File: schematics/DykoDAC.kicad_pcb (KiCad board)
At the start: 2 copper layers, 99.2 x 99.8 mm, 147 parts, among them J1 AC Input, J2 AudioJack, J3 USB_B, J4 OLED, J5 Debug, J6 Conn_01x05, J7 Conn_01x04, J8 Conn_01x05, J9 Conn_01x04, SW1 EC11B152420G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

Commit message: update
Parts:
- added C70: 10u, Capacitor_Tantalum_SMD:CP_EIA-3216-18_Kemet-A, F.Cu at (95.4, 135.4)
- C14, C15, C26, C29, C33, C35, C42, C50, C52, C59, C64, C65, C9: footprint Capacitors_Tantalum_SMD:CP_Tantalum_Case-A_EIA-3216-18_Reflow -> Capacitor_Tantalum_SMD:CP_EIA-3216-18_Kemet-A
- C32, C49, C7, C8: footprint Capacitors_Tantalum_SMD:CP_Tantalum_Case-D_EIA-7343-31_Reflow -> Capacitor_Tantalum_SMD:CP_EIA-7343-31_Kemet-D
- J2: footprint Connect:Stereo_Jack_3.5mm_Switch_Ledino_KB3SPRS -> kamtar:StereoJack_3.5mm_Lumberg
- moved L3 0.66 mm to (93.5, 134.7)
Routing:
- net +3V3: track 137.7 -> 157.8 mm
- net Net-(J2-Pad3): track 33.5 -> 21.9 mm
- net Net-(J2-Pad2): track 12.4 -> 21.5 mm
- net GND: track 105.2 -> 107.9 mm, vias 694 -> 878
- net /DykoDAC_CS4398/3V3_CS: track 30.5 -> 29.9 mm
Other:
- board text added: "Kamtar 2020"
- board text removed: "Kamtar 2019"

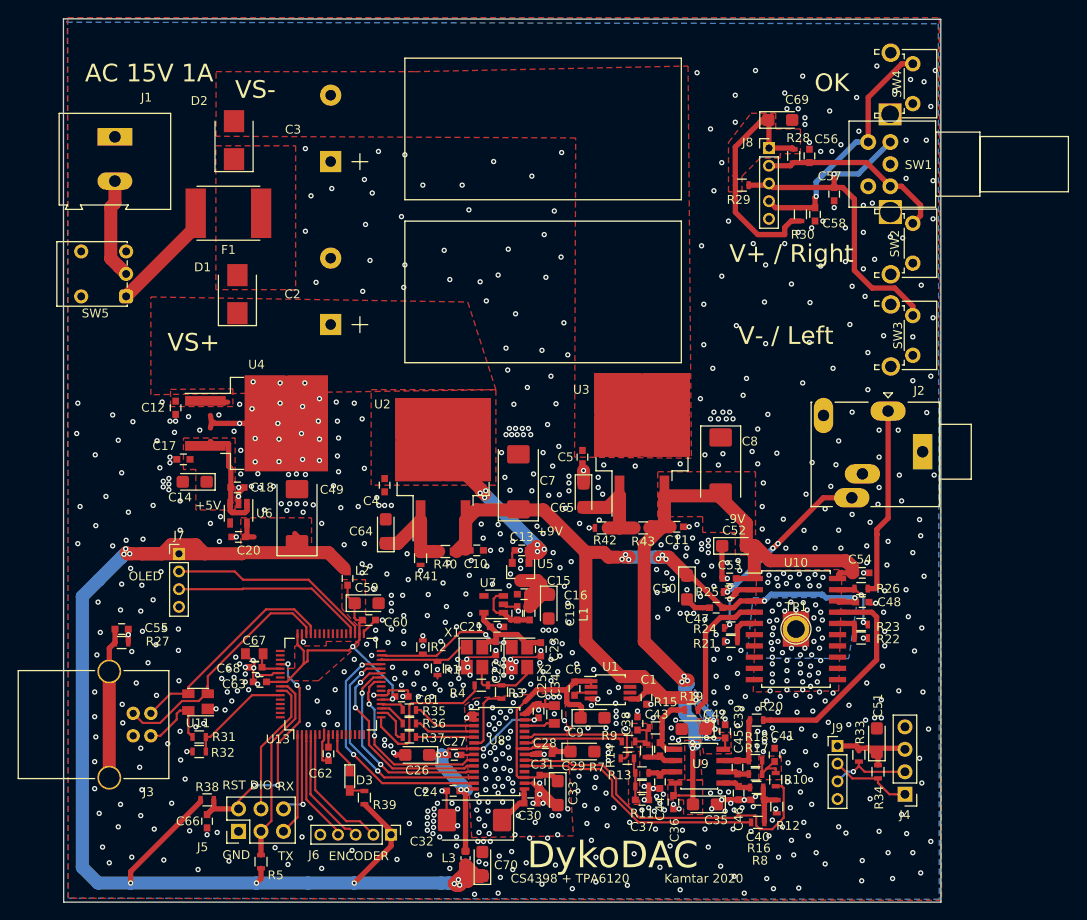
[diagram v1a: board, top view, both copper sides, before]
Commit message: lm317 fix
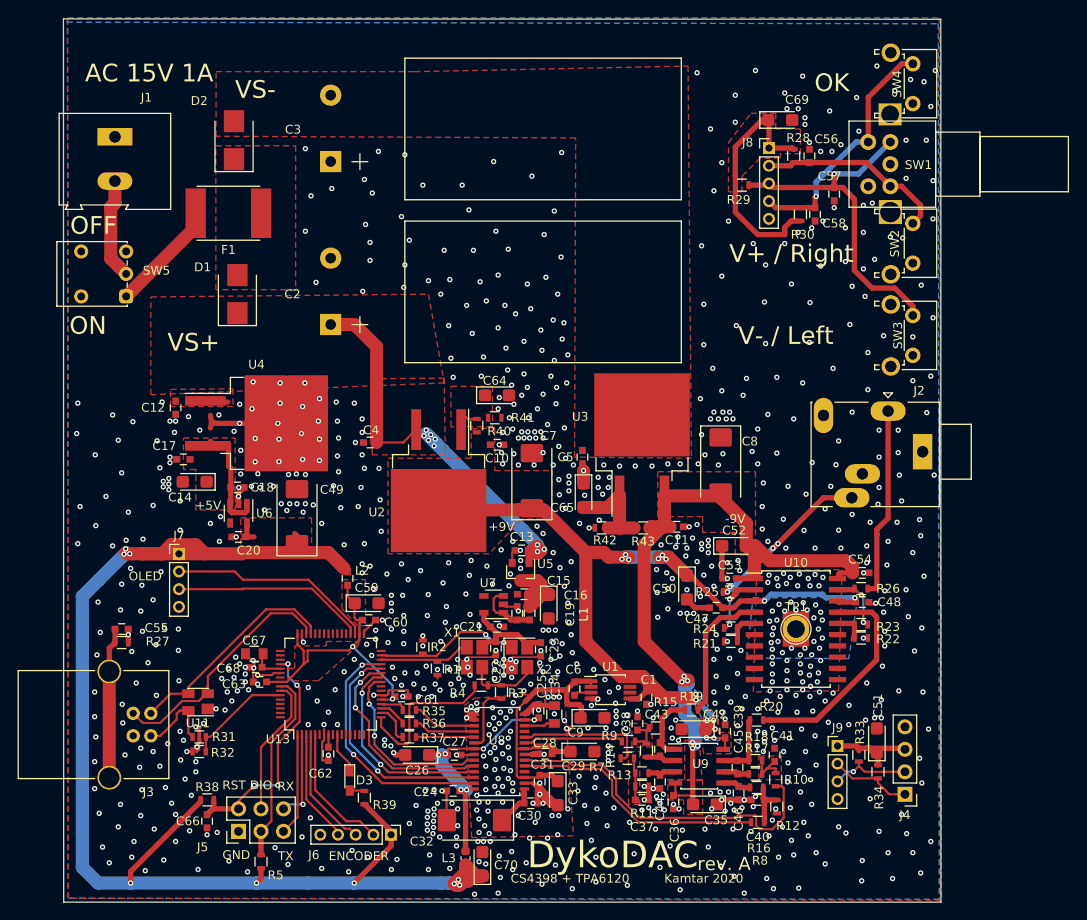
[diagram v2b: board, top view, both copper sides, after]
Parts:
- SW5: value SW_SPDT -> PWR_SWITCH
- U2, U3: footprint TO_SOT_Packages_SMD:TO-263-2 -> Package_TO_SOT_SMD:TO-263-2
- moved C64 19.9 mm to (97.0, 82.4), turned to 0 degrees
- moved R41 18.0 mm to (96.8, 85.0), turned to 0 degrees
- moved R40 14.7 mm to (94.7, 85.9), turned to 90 degrees
- moved C10 12.2 mm to (97.0, 88.0)
- moved C4 5.10 mm to (82.7, 87.8), turned to 180 degrees
- moved C7 1.53 mm to (101.0, 92.1)
- moved U2 1.37 mm to (90.4, 92.1), turned to 270 degrees
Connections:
- U2 pad 2: VS_POS -> +9V
- U2 pad 3: +9V -> VS_POS
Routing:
- net VS_POS: track 19.4 -> 46.4 mm, vias 6 -> 9
- net GND: track 107.9 -> 118.2 mm, vias 878 -> 954
- net +9V: track 110.9 -> 102.0 mm
- net Net-(C64-Pad1): track 10.6 -> 4.07 mm
- added copper zone on F.Cu, net Net-(C64-Pad1)
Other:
- board text added: "OFF"
- board text added: "ON"
- board text added: "rev. A"

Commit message: updated fuse
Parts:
- F1: footprint Fuse_Holders_and_Fuses:Fuse_SMD2920 -> kamtar:UNIFuse_SMD2920
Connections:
- J2 pad 4: Net-(J2-Pad4) -> (no net)
- J2 pad 5: Net-(J2-Pad5) -> (no net)
- SW5 pad 3: Net-(SW5-Pad3) -> (no net)
- U1 pad 6: Net-(U1-Pad6) -> (no net)
- U1 pad 7: Net-(U1-Pad7) -> (no net)
- U13 pad 11: Net-(U13-Pad11) -> (no net)
- U13 pad 12: Net-(U13-Pad12) -> (no net)
- U13 pad 13: Net-(U13-Pad13) -> (no net)
- U13 pad 14: Net-(U13-Pad14) -> (no net)
- U13 pad 15: Net-(U13-Pad15) -> (no net)
- U13 pad 16: Net-(U13-Pad16) -> (no net)
- U13 pad 23: Net-(U13-Pad23) -> (no net)
- U13 pad 24: Net-(U13-Pad24) -> (no net)
- U13 pad 32: Net-(U13-Pad32) -> (no net)
- U13 pad 37: Net-(U13-Pad37) -> (no net)
- U13 pad 38: Net-(U13-Pad38) -> (no net)
- U13 pad 39: Net-(U13-Pad39) -> (no net)
- U13 pad 40: Net-(U13-Pad40) -> (no net)
- U13 pad 41: Net-(U13-Pad41) -> (no net)
- U13 pad 42: Net-(U13-Pad42) -> (no net)
- U13 pad 43: Net-(U13-Pad43) -> (no net)
- U13 pad 44: Net-(U13-Pad44) -> (no net)
- U13 pad 49: Net-(U13-Pad49) -> (no net)
- U13 pad 50: Net-(U13-Pad50) -> (no net)
- U13 pad 51: Net-(U13-Pad51) -> (no net)
- U13 pad 55: Net-(U13-Pad55) -> (no net)
- U13 pad 6: Net-(U13-Pad6) -> (no net)
- U13 pad 60: Net-(U13-Pad60) -> (no net)
- U13 pad 61: Net-(U13-Pad61) -> (no net)
- U13 pad 62: Net-(U13-Pad62) -> (no net)
- U13 pad 63: Net-(U13-Pad63) -> (no net)
- U13 pad 64: Net-(U13-Pad64) -> (no net)
- U13 pad 9: Net-(U13-Pad9) -> (no net)
- U6 pad 4: Net-(U6-Pad4) -> (no net)
- U7 pad 4: Net-(U7-Pad4) -> (no net)
- U8 pad 18: Net-(U8-Pad18) -> (no net)
- U8 pad 25: Net-(U8-Pad25) -> (no net)
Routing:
- net GND: vias 954 -> 957

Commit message: added vias
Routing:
- net GND: vias 957 -> 960
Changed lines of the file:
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@@
     (thickness 1.6)
     (drawings 26)
-    (tracks 2032)
+    (tracks 2035)
     (zones 0)
     (modules 148)
@@
       (padsonsilk false)
       (subtractmaskfromsilk false)
-      (outputformat 1)
+      (outputformat 4)
       (mirror false)
       (drillshape 0)
@@
     (add_net "Net-(J2-Pad2)")
     (add_net "Net-(J2-Pad3)")
-    (add_net "Net-(J2-Pad4)")
-    (add_net "Net-(J2-Pad5)")
     (add_net "Net-(J3-Pad1)")
     (add_net "Net-(J4-Pad1)")
@@
     (add_net "Net-(R36-Pad1)")
     (add_net "Net-(R37-Pad1)")
-    (add_net "Net-(SW5-Pad3)")
-    (add_net "Net-(U1-Pad6)")
-    (add_net "Net-(U1-Pad7)")
-    (add_net "Net-(U13-Pad11)")
-    (add_net "Net-(U13-Pad12)")
-    (add_net "Net-(U13-Pad13)")
-    (add_net "Net-(U13-Pad14)")
-    (add_net "Net-(U13-Pad15)")
-    (add_net "Net-(U13-Pad16)")
-    (add_net "Net-(U13-Pad23)")
-    (add_net "Net-(U13-Pad24)")
-    (add_net "Net-(U13-Pad32)")
-    (add_net "Net-(U13-Pad37)")
-    (add_net "Net-(U13-Pad38)")
-    (add_net "Net-(U13-Pad39)")
-    (add_net "Net-(U13-Pad40)")
-    (add_net "Net-(U13-Pad41)")
-    (add_net "Net-(U13-Pad42)")
-    (add_net "Net-(U13-Pad43)")
-    (add_net "Net-(U13-Pad44)")
-    (add_net "Net-(U13-Pad49)")
-    (add_net "Net-(U13-Pad50)")
-    (add_net "Net-(U13-Pad51)")
-    (add_net "Net-(U13-Pad55)")
-    (add_net "Net-(U13-Pad6)")
-    (add_net "Net-(U13-Pad60)")
-    (add_net "Net-(U13-Pad61)")
-    (add_net "Net-(U13-Pad62)")
-    (add_net "Net-(U13-Pad63)")
-    (add_net "Net-(U13-Pad64)")
-    (add_net "Net-(U13-Pad9)")
-    (add_net "Net-(U6-Pad4)")
-    (add_net "Net-(U7-Pad4)")
-    (add_net "Net-(U8-Pad18)")
-    (add_net "Net-(U8-Pad25)")
     (add_net OSC_EN_1)
     (add_net OSC_EN_2)
@@
   (via (at 128.397 121.412) (size 0.6) (drill 0.3) (layers F.Cu B.Cu) (net 1))
   (via (at 128.524 129.159) (size 0.6) (drill 0.3) (layers F.Cu B.Cu) (net 1))
-  (via (at 109.601 122.047) (size 0.6) (drill 0.3) (layers F.Cu B.Cu) (net 1))
-  (via (at 109.601 122.809) (size 0.6) (drill 0.3) (layers F.Cu B.Cu) (net 1))
-  (via (at 109.601 123.698) (size 0.6) (drill 0.3) (layers F.Cu B.Cu) (net 1))
+  (via (at 109.4232 122.0216) (size 0.6) (drill 0.3) (layers F.Cu B.Cu) (net 1))
+  (via (at 109.347 122.809) (size 0.6) (drill 0.3) (layers F.Cu B.Cu) (net 1))
+  (via (at 109.3724 123.5456) (size 0.6) (drill 0.3) (layers F.Cu B.Cu) (net 1))
   (via (at 110.49 119.507) (size 0.6) (drill 0.3) (layers F.Cu B.Cu) (net 1))
   (via (at 110.49 118.745) (size 0.6) (drill 0.3) (layers F.Cu B.Cu) (net 1))
@@
   (via (at 139.7508 121.412) (size 0.6) (drill 0.3) (layers F.Cu B.Cu) (net 1))
   (via (at 141.5796 121.3612) (size 0.6) (drill 0.3) (layers F.Cu B.Cu) (net 1))
+  (via (at 106.934 121.9708) (size 0.6) (drill 0.3) (layers F.Cu B.Cu) (net 1))
+  (via (at 106.934 122.682) (size 0.6) (drill 0.3) (layers F.Cu B.Cu) (net 1))
+  (via (at 106.934 123.3932) (size 0.6) (drill 0.3) (layers F.Cu B.Cu) (net 1))
   (segment (start 122.797 122.219) (end 122.588 122.428) (width 0.25) (layer F.Cu) (net 2))
   (segment (start 122.184 121.146) (end 122.809 121.146) (width 0.25) (layer F.Cu) (net 2))

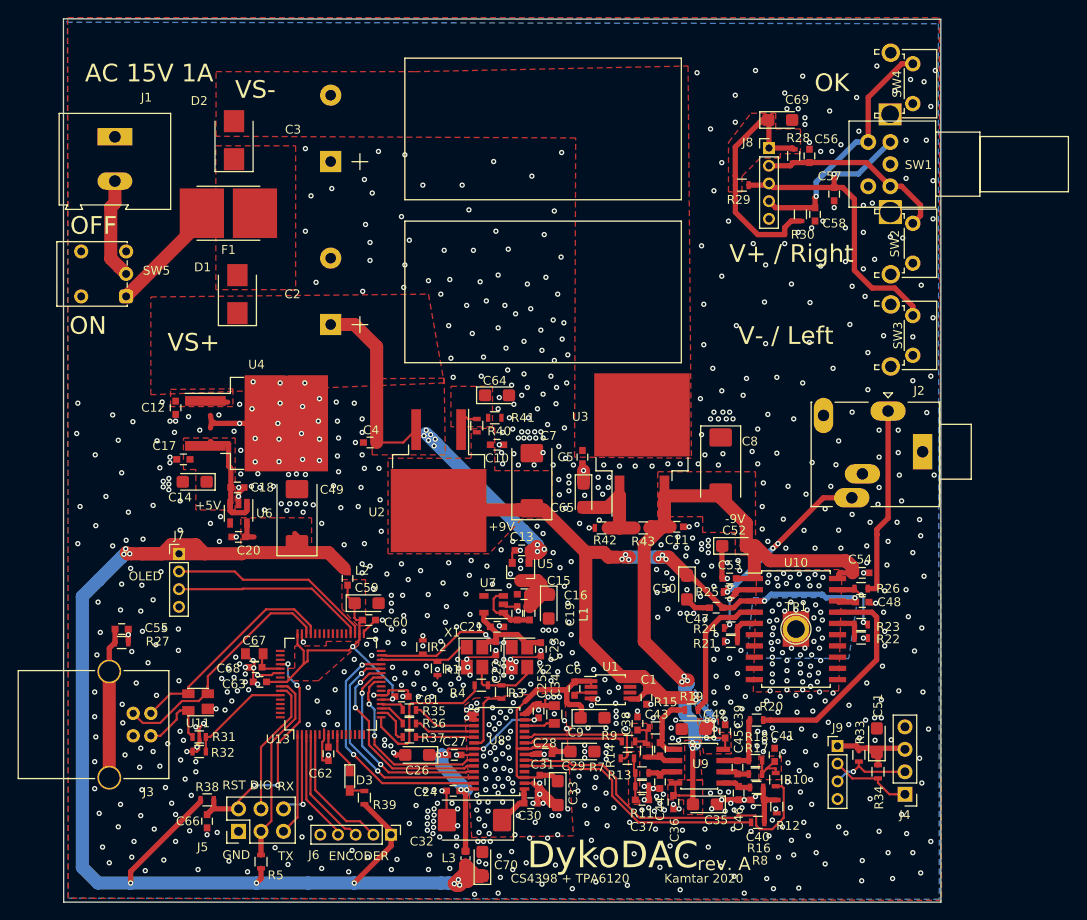
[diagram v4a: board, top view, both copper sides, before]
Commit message: ldo change
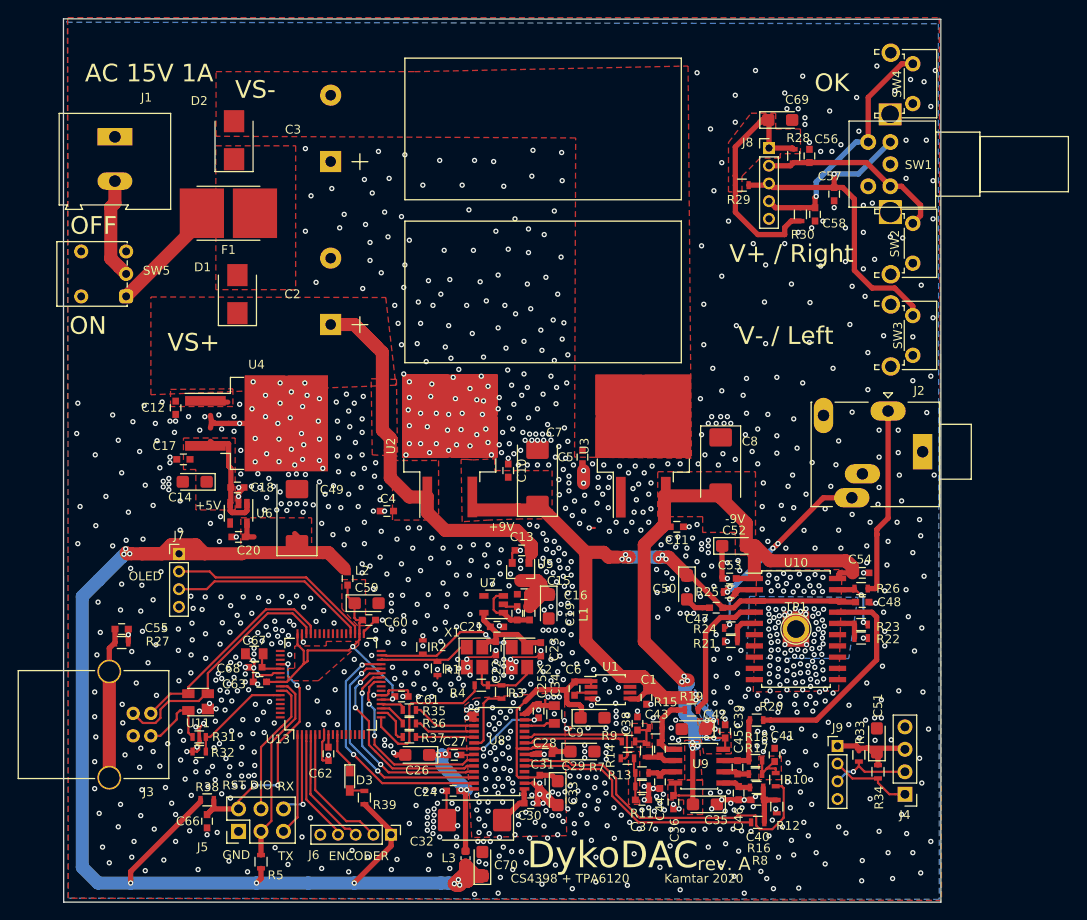
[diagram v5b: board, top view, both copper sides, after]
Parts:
- removed C64, C65: 10u, Capacitor_Tantalum_SMD:CP_EIA-3216-18_Kemet-A
- removed R40, R43: 240, Resistors_SMD:R_0603
- removed R41, R42: 1k5, Resistors_SMD:R_0603
- U2: value LM317 -> L7812; footprint Package_TO_SOT_SMD:TO-263-2 -> TO_SOT_Packages_SMD:TO-263-2
- U3: value LM337 -> L7912; footprint Package_TO_SOT_SMD:TO-263-2 -> TO_SOT_Packages_SMD:TO-263-2
- moved C4 7.98 mm to (84.6, 95.5)
- moved U2 4.14 mm to (91.7, 88.1), turned to 90 degrees
- moved C10 3.19 mm to (98.3, 90.9), turned to 90 degrees
- moved C7 0.74 mm to (101.6, 91.7)
- moved U3 0.22 mm to (113.6, 88.2)
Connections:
- U2 pad 1: Net-(C64-Pad1) -> VS_POS
- U2 pad 2: +9V -> GND
- U2 pad 3: VS_POS -> +9V
- U3 pad 1: Net-(C65-Pad2) -> GND
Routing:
- net Net-(C65-Pad2): track 11.2 -> 0.00 mm
- net GND: track 118.2 -> 124.3 mm, vias 960 -> 1301
- net Net-(C64-Pad1): track 4.07 -> 0.00 mm
- net VS_POS: track 46.4 -> 50.0 mm, vias 9 -> 0
- net -9V: track 88.5 -> 86.2 mm
- net +9V: track 102.0 -> 100.3 mm, vias 15 -> 13
- net /DykoDAC_MCU/OLED_SCL: track 21.9 -> 22.6 mm

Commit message: PRODUCTION - REV A
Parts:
- moved C4 3.09 mm to (87.5, 96.5), turned to 270 degrees
- moved C7 1.40 mm to (101.7, 90.3)
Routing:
- net GND: track 124.3 -> 126.1 mm, vias 1301 -> 1424
- net 3V3_OSC: track 12.0 -> 13.5 mm
- removed copper zone on F.Cu, net Net-(C64-Pad1)
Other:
- board text added: "JLCJLCJLCJLC"
